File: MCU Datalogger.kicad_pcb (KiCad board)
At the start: 2 copper layers, 2 parts, among them U3 DS1337S_, U4 ATmega328P-A

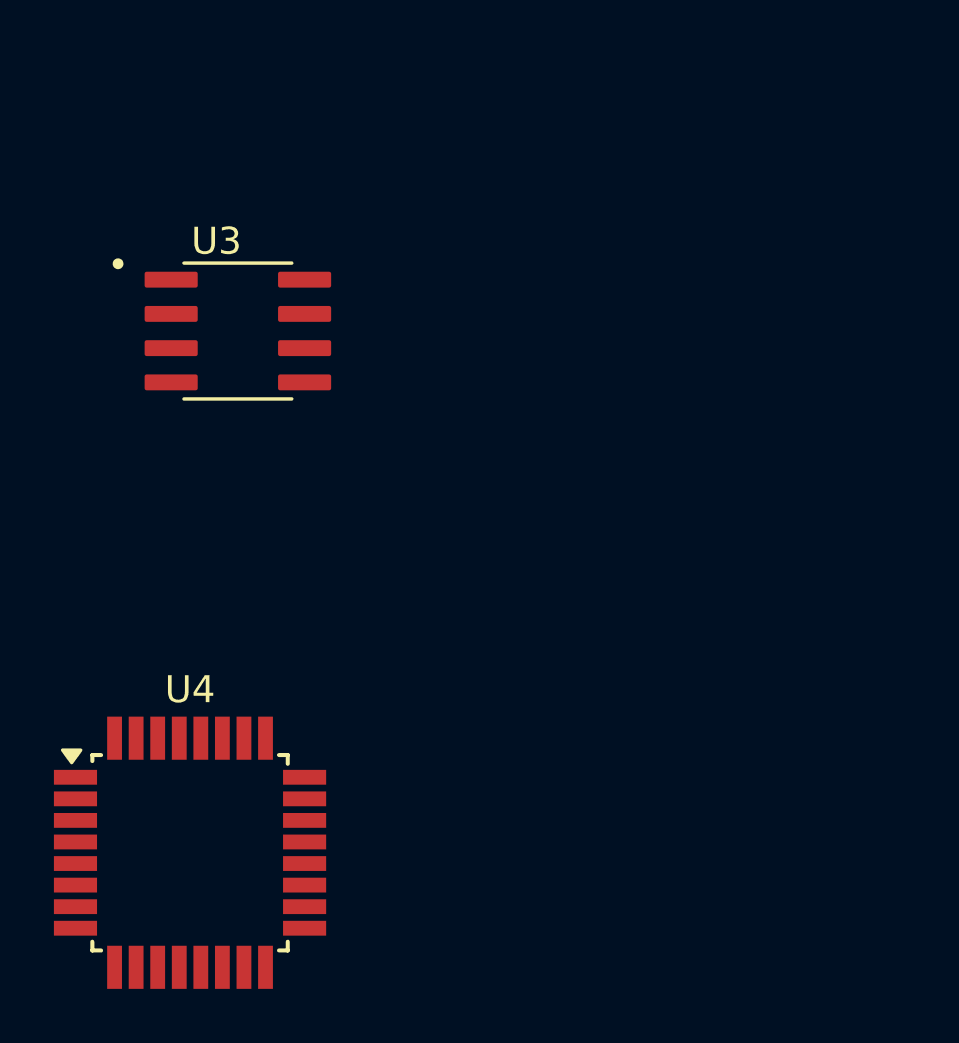
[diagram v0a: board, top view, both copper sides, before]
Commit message: updating the project with all necessary component libraries
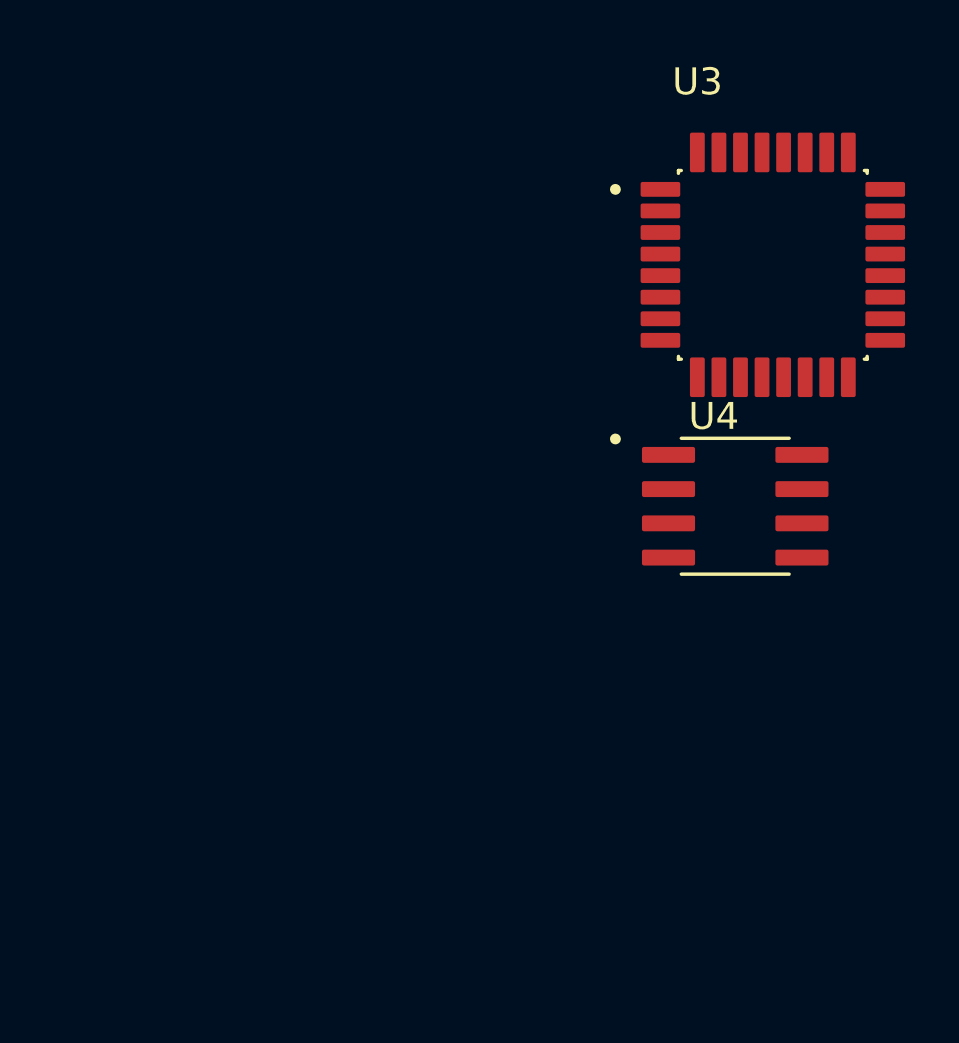
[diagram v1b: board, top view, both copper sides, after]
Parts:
- U3: value DS1337S_ -> ATMEGA328P-AU; footprint DS1337S_:SOIC127P600X175-8N -> ATMEGA328P-AU:QFP80P900X900X120-32N
- U4: value ATmega328P-A -> DS1337S_; footprint Package_QFP:TQFP-32_7x7mm_P0.8mm -> DS1337S_:SOIC127P600X175-8N
- moved U4 24.0 mm to (149.5, 88.1)
- moved U3 20.0 mm to (150.9, 79.1)
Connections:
- U3 pad 3: unconnected-(U3-~{INTA}-Pad3) -> Net-(U3-GND-Pad21)
- U3 pad 4: unconnected-(U3-GND-Pad4) -> Net-(U3-VCC-Pad4)
- U3 pad 5: unconnected-(U3-SDA-Pad5) -> Net-(U3-GND-Pad21)
- U3 pad 6: unconnected-(U3-SCL-Pad6) -> Net-(U3-VCC-Pad4)
- U4 pad 3: Net-(U4-GND-Pad21) -> unconnected-(U4-~{INTA}-Pad3)
- U4 pad 4: Net-(U4-VCC-Pad4) -> unconnected-(U4-GND-Pad4)
- U4 pad 5: Net-(U4-GND-Pad21) -> unconnected-(U4-SDA-Pad5)
- U4 pad 6: Net-(U4-VCC-Pad4) -> unconnected-(U4-SCL-Pad6)

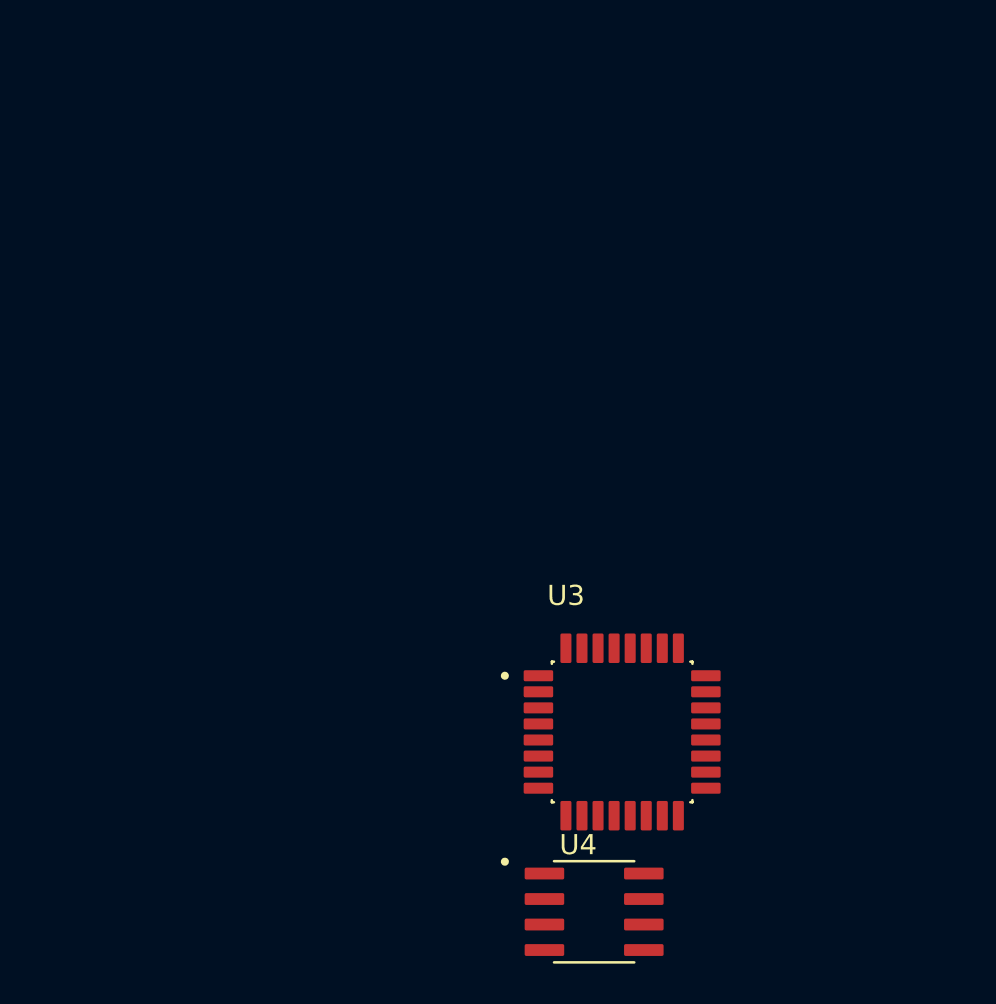
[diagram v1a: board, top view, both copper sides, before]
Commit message: proceeded to wire all the components on the first sheet
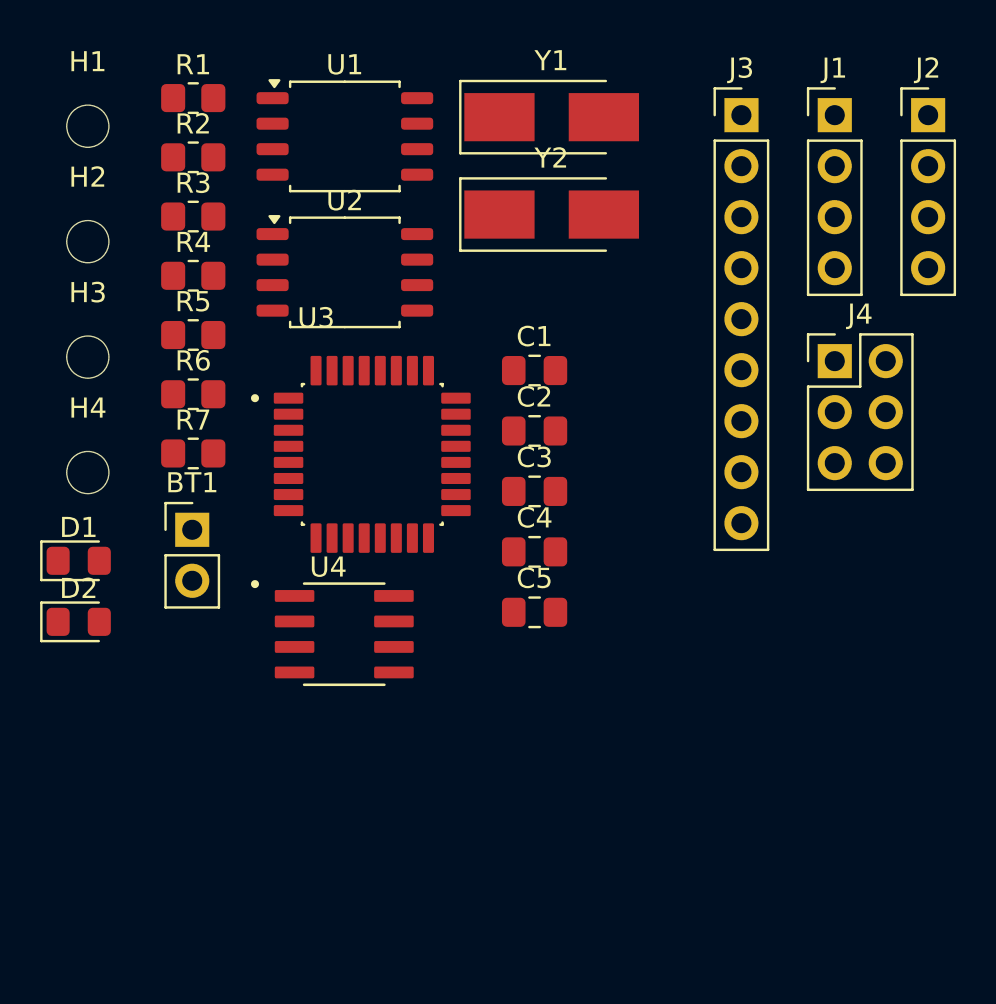
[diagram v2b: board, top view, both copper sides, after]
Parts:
- added BT1: Battery, Connector_PinHeader_2.54mm:PinHeader_1x02_P2.54mm_Vertical, F.Cu at (129.5, 69.1)
- added C1: 0.1u, Capacitor_SMD:C_0805_2012Metric_Pad1.18x1.45mm_HandSolder, F.Cu at (146.5, 61.1)
- added C2: 0.1u, Capacitor_SMD:C_0805_2012Metric_Pad1.18x1.45mm_HandSolder, F.Cu at (146.5, 64.2)
- added C3: 22pF, Capacitor_SMD:C_0805_2012Metric_Pad1.18x1.45mm_HandSolder, F.Cu at (146.5, 67.2)
- added C4: 22pF, Capacitor_SMD:C_0805_2012Metric_Pad1.18x1.45mm_HandSolder, F.Cu at (146.5, 70.2)
- added C5: 100nF, Capacitor_SMD:C_0805_2012Metric_Pad1.18x1.45mm_HandSolder, F.Cu at (146.5, 73.2)
- added D1: LED, LED_SMD:LED_0805_2012Metric_Pad1.15x1.40mm_HandSolder, F.Cu at (123.8, 70.6)
- added D2: LED, LED_SMD:LED_0805_2012Metric_Pad1.15x1.40mm_HandSolder, F.Cu at (123.8, 73.7)
- added H1: MountingHole, MountingHole:MountingHole_2.1mm, F.Cu at (124.3, 49.0)
- added H2: MountingHole, MountingHole:MountingHole_2.1mm, F.Cu at (124.3, 54.7)
- added H3: MountingHole, MountingHole:MountingHole_2.1mm, F.Cu at (124.3, 60.5)
- added H4: MountingHole, MountingHole:MountingHole_2.1mm, F.Cu at (124.3, 66.2)
- added J1: Conn_01x04_Pin, Connector_PinHeader_2.54mm:PinHeader_1x04_P2.54mm_Vertical, F.Cu at (161.5, 48.4)
- added J2: Conn_01x04_Pin, Connector_PinHeader_2.54mm:PinHeader_1x04_P2.54mm_Vertical, F.Cu at (166.1, 48.4)
- added J3: Conn_01x09_Pin, Connector_PinHeader_2.54mm:PinHeader_1x09_P2.54mm_Vertical, F.Cu at (156.8, 48.4)
- added J4: Conn_02x03_Odd_Even, Connector_PinHeader_2.54mm:PinHeader_2x03_P2.54mm_Vertical, F.Cu at (161.5, 60.7)
- added R1: 10K, Resistor_SMD:R_0805_2012Metric_Pad1.20x1.40mm_HandSolder, F.Cu at (129.5, 47.6)
- added R2: 10K, Resistor_SMD:R_0805_2012Metric_Pad1.20x1.40mm_HandSolder, F.Cu at (129.5, 50.5)
- added R3: 4.7K, Resistor_SMD:R_0805_2012Metric_Pad1.20x1.40mm_HandSolder, F.Cu at (129.5, 53.5)
- added R4: 4.7K, Resistor_SMD:R_0805_2012Metric_Pad1.20x1.40mm_HandSolder, F.Cu at (129.5, 56.4)
- added R5: 330, Resistor_SMD:R_0805_2012Metric_Pad1.20x1.40mm_HandSolder, F.Cu at (129.5, 59.4)
- added R6: 330, Resistor_SMD:R_0805_2012Metric_Pad1.20x1.40mm_HandSolder, F.Cu at (129.5, 62.3)
- added R7: 10K, Resistor_SMD:R_0805_2012Metric_Pad1.20x1.40mm_HandSolder, F.Cu at (129.5, 65.3)
- added U1: 24LC1025, Package_SO:SOIC-8_5.23x5.23mm_P1.27mm, F.Cu at (137.1, 49.5)
- added U2: 24LC1025, Package_SO:SOIC-8_5.23x5.23mm_P1.27mm, F.Cu at (137.1, 56.2)
- added Y1: 32.768kHz, Crystal:Crystal_SMD_5032-2Pin_5.0x3.2mm_HandSoldering, F.Cu at (147.4, 48.5)
- added Y2: 16KHz, Crystal:Crystal_SMD_5032-2Pin_5.0x3.2mm_HandSoldering, F.Cu at (147.4, 53.4)
- moved U3 18.6 mm to (138.4, 65.3)
- moved U4 18.6 mm to (137.0, 74.3)

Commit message: fixed gitignore patterns
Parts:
- moved U2 36.7 mm to (103.2, 70.5)
- moved U1 34.6 mm to (102.5, 51.5)
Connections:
- BT1 pad 1: unconnected-(BT1-+-Pad1) -> /Vcc
- BT1 pad 2: unconnected-(BT1---Pad2) -> GND
- C1 pad 1: unconnected-(C1-Pad1) -> /Vcc
- C1 pad 2: unconnected-(C1-Pad2) -> GND
- C2 pad 1: unconnected-(C2-Pad1) -> Net-(U3-AREF)
- C2 pad 2: unconnected-(C2-Pad2) -> GND
- C3 pad 1: unconnected-(C3-Pad1) -> GND
- C3 pad 2: unconnected-(C3-Pad2) -> Net-(U3-PB6)
- C4 pad 1: unconnected-(C4-Pad1) -> Net-(U3-PB7)
- C4 pad 2: unconnected-(C4-Pad2) -> GND
- C5 pad 1: unconnected-(C5-Pad1) -> /Vcc
- C5 pad 2: unconnected-(C5-Pad2) -> GND
- D1 pad 1: unconnected-(D1-K-Pad1) -> Net-(D1-K)
- D1 pad 2: unconnected-(D1-A-Pad2) -> /Vcc
- D2 pad 1: unconnected-(D2-K-Pad1) -> Net-(D2-K)
- D2 pad 2: unconnected-(D2-A-Pad2) -> /SCK
- J1 pad 1: unconnected-(J1-Pin_1-Pad1) -> GND
- J1 pad 2: unconnected-(J1-Pin_2-Pad2) -> /Vcc
- J1 pad 3: unconnected-(J1-Pin_3-Pad3) -> /SDA
- J1 pad 4: unconnected-(J1-Pin_4-Pad4) -> /SCK
- J2 pad 1: unconnected-(J2-Pin_1-Pad1) -> GND
- J2 pad 2: unconnected-(J2-Pin_2-Pad2) -> /Vcc
- J2 pad 3: unconnected-(J2-Pin_3-Pad3) -> /RX
- J2 pad 4: unconnected-(J2-Pin_4-Pad4) -> /TX
- J3 pad 1: unconnected-(J3-Pin_1-Pad1) -> /D2
- J3 pad 2: unconnected-(J3-Pin_2-Pad2) -> /D3
- J3 pad 3: unconnected-(J3-Pin_3-Pad3) -> /D4
- J3 pad 4: unconnected-(J3-Pin_4-Pad4) -> /D5
- J3 pad 5: unconnected-(J3-Pin_5-Pad5) -> /D6
- J3 pad 6: unconnected-(J3-Pin_6-Pad6) -> /D7
- J3 pad 7: unconnected-(J3-Pin_7-Pad7) -> /D8
- J3 pad 8: unconnected-(J3-Pin_8-Pad8) -> /Vcc
- J3 pad 9: unconnected-(J3-Pin_9-Pad9) -> GND
- J4 pad 1: unconnected-(J4-Pin_1-Pad1) -> /MISO
- J4 pad 2: unconnected-(J4-Pin_2-Pad2) -> /Vcc
- J4 pad 3: unconnected-(J4-Pin_3-Pad3) -> /SCK
- J4 pad 4: unconnected-(J4-Pin_4-Pad4) -> /MOSI
- J4 pad 5: unconnected-(J4-Pin_5-Pad5) -> /RESET
- J4 pad 6: unconnected-(J4-Pin_6-Pad6) -> GND
- R1 pad 1: unconnected-(R1-Pad1) -> /Vcc
- R1 pad 2: unconnected-(R1-Pad2) -> Net-(U4-SQW/~INT)
- R2 pad 1: unconnected-(R2-Pad1) -> /Vcc
- R2 pad 2: unconnected-(R2-Pad2) -> Net-(U4-~{INTA})
- R3 pad 1: unconnected-(R3-Pad1) -> /Vcc
- R3 pad 2: unconnected-(R3-Pad2) -> /SCK
- R4 pad 1: unconnected-(R4-Pad1) -> /SDA
- R4 pad 2: unconnected-(R4-Pad2) -> /Vcc
- R5 pad 1: unconnected-(R5-Pad1) -> Net-(D1-K)
- R5 pad 2: unconnected-(R5-Pad2) -> GND
- R6 pad 1: unconnected-(R6-Pad1) -> GND
- R6 pad 2: unconnected-(R6-Pad2) -> Net-(D2-K)
- R7 pad 1: unconnected-(R7-Pad1) -> /RESET
- R7 pad 2: unconnected-(R7-Pad2) -> /Vcc
- U1 pad 1: unconnected-(U1-A0-Pad1) -> /Vcc
- U1 pad 2: unconnected-(U1-A1-Pad2) -> /Vcc
- U1 pad 3: unconnected-(U1-A2-Pad3) -> /Vcc
- U1 pad 4: unconnected-(U1-GND-Pad4) -> GND
- U1 pad 5: unconnected-(U1-SDA-Pad5) -> /SDA
- U1 pad 6: unconnected-(U1-SCL-Pad6) -> /SCK
- U1 pad 7: unconnected-(U1-WP-Pad7) -> GND
- U1 pad 8: unconnected-(U1-VCC-Pad8) -> /Vcc
- U2 pad 1: unconnected-(U2-A0-Pad1) -> /Vcc
- U2 pad 2: unconnected-(U2-A1-Pad2) -> GND
- U2 pad 3: unconnected-(U2-A2-Pad3) -> /Vcc
- U2 pad 4: unconnected-(U2-GND-Pad4) -> GND
- U2 pad 5: unconnected-(U2-SDA-Pad5) -> /SDA
- U2 pad 6: unconnected-(U2-SCL-Pad6) -> /SCK
- U2 pad 7: unconnected-(U2-WP-Pad7) -> GND
- U2 pad 8: unconnected-(U2-VCC-Pad8) -> /Vcc
- U3 pad 1: unconnected-(U3-PD3-Pad1) -> /D3
- U3 pad 10: unconnected-(U3-PD6-Pad10) -> /D6
- U3 pad 11: unconnected-(U3-PD7-Pad11) -> /D7
- U3 pad 12: unconnected-(U3-PB0-Pad12) -> /D8
- U3 pad 15: unconnected-(U3-PB3-Pad15) -> /MOSI
- U3 pad 16: unconnected-(U3-PB4-Pad16) -> /MISO
- U3 pad 17: unconnected-(U3-PB5-Pad17) -> /SCK
- U3 pad 18: unconnected-(U3-AVCC-Pad18) -> /Vcc
- U3 pad 2: unconnected-(U3-PD4-Pad2) -> /D4
- U3 pad 20: unconnected-(U3-AREF-Pad20) -> Net-(U3-AREF)
- U3 pad 21: Net-(U3-GND-Pad21) -> GND
- U3 pad 27: unconnected-(U3-PC4-Pad27) -> /SDA
- U3 pad 28: unconnected-(U3-PC5-Pad28) -> /SCK
- U3 pad 29: unconnected-(U3-PC6/~{RESET}-Pad29) -> /RESET
- U3 pad 3: Net-(U3-GND-Pad21) -> GND
- U3 pad 30: unconnected-(U3-PD0-Pad30) -> /RX
- U3 pad 31: unconnected-(U3-PD1-Pad31) -> /TX
- U3 pad 32: unconnected-(U3-PD2-Pad32) -> /D2
- U3 pad 4: Net-(U3-VCC-Pad4) -> /Vcc
- U3 pad 5: Net-(U3-GND-Pad21) -> GND
- U3 pad 6: Net-(U3-VCC-Pad4) -> unconnected-(U3-VCC-Pad6)
- U3 pad 7: unconnected-(U3-PB6-Pad7) -> Net-(U3-PB6)
- U3 pad 8: unconnected-(U3-PB7-Pad8) -> Net-(U3-PB7)
- U3 pad 9: unconnected-(U3-PD5-Pad9) -> /D5
- U4 pad 1: unconnected-(U4-X1-Pad1) -> Net-(U4-X1)
- U4 pad 2: unconnected-(U4-X2-Pad2) -> Net-(U4-X2)
- U4 pad 3: unconnected-(U4-~{INTA}-Pad3) -> Net-(U4-~{INTA})
- U4 pad 4: unconnected-(U4-GND-Pad4) -> GND
- U4 pad 5: unconnected-(U4-SDA-Pad5) -> /SDA
- U4 pad 6: unconnected-(U4-SCL-Pad6) -> /SCK
- U4 pad 7: unconnected-(U4-SQW/~INT-Pad7) -> Net-(U4-SQW/~INT)
- U4 pad 8: unconnected-(U4-VCC-Pad8) -> /Vcc
- Y1 pad 1: unconnected-(Y1-Pad1) -> Net-(U4-X2)
- Y1 pad 2: unconnected-(Y1-Pad2) -> Net-(U4-X1)
- Y2 pad 1: unconnected-(Y2-Pad1) -> Net-(U3-PB7)
- Y2 pad 2: unconnected-(Y2-Pad2) -> Net-(U3-PB6)

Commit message: commited the placement of components
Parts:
- moved J3 101.6 mm to (93.7, 128.0), turned to 90 degrees
- moved J2 92.9 mm to (118.1, 128.0), turned to 90 degrees
- moved Y1 89.9 mm to (94.6, 121.3), turned to 90 degrees
- moved J4 88.9 mm to (87.0, 109.2)
- moved R2 79.9 mm to (98.8, 124.3), turned to 180 degrees
- moved H3 76.7 mm to (87.6, 127.9)
- moved R1 75.7 mm to (106.8, 119.8), turned to -90 degrees
- moved C5 73.2 mm to (90.9, 120.8), turned to -90 degrees
- moved Y2 72.2 mm to (116.5, 118.6), turned to 180 degrees
- moved C1 70.9 mm to (102.2, 116.5), turned to 180 degrees
- moved J1 68.5 mm to (133.0, 110.7)
- moved H1 65.6 mm to (87.8, 103.5)
- moved BT1 65.6 mm to (87.6, 119.6)
- moved C3 63.7 mm to (114.4, 122.2), turned to 180 degrees
- moved H4 62.5 mm to (132.6, 128.1)
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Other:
- board outline added: 50 x 30 mm
